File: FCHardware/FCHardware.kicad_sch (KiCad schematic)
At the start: 40 parts, among them J1 JST-8pin, J3 USB_C_Receptacle_USB2.0_16P, SW3 SW_Push, U2 MPU-6050, U4 TPSM63603, U5 ESC_Xrotor_65A_4in1, U8 ESP32-S3-MINI-1U, U9 USBLC6-2SC6

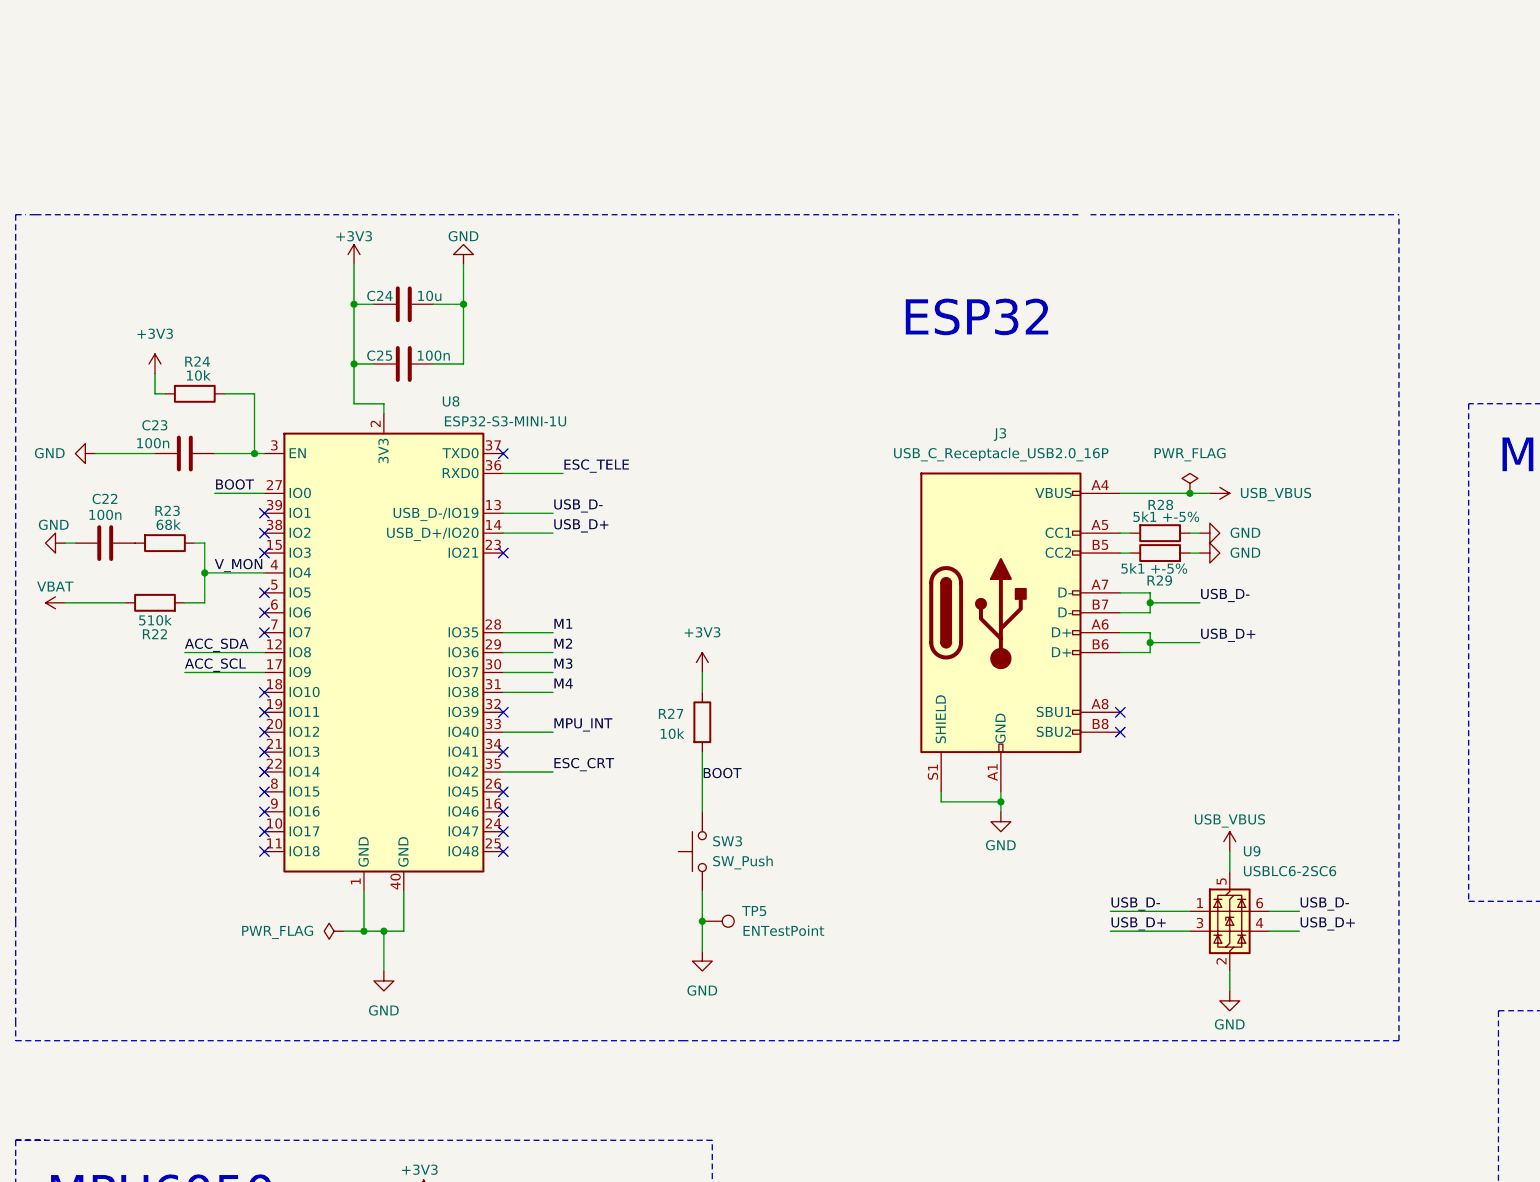
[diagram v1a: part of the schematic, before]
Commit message: Added actual references to capacitors and resistors
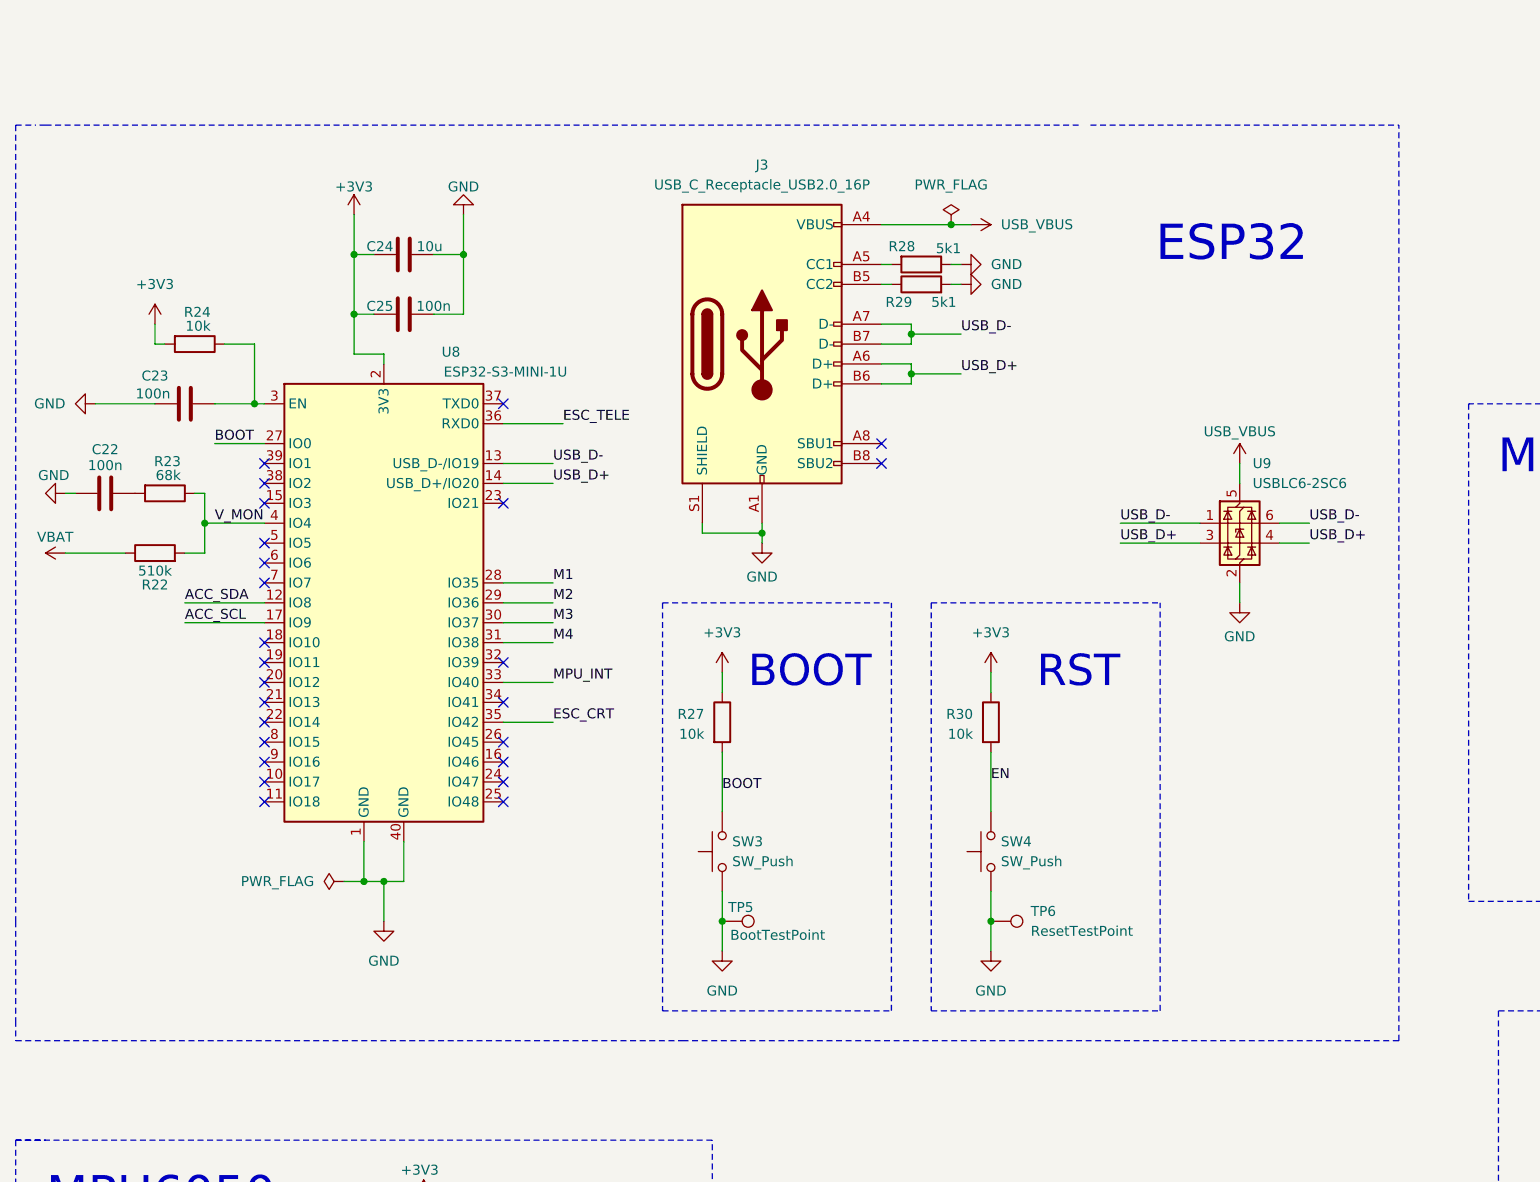
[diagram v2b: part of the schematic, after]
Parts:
- added R30: 10k, Resistor_SMD:R_0603_1608Metric_Pad0.98x0.95mm_HandSolder, symbol Device:R
- added SW4: SW_Push, Button_Switch_THT:SW_PUSH_6mm, symbol Switch:SW_Push
- added TP6: ResetTestPoint, TestPoint:TestPoint_Pad_D1.5mm, symbol Connector:TestPoint
- R28, R29: value 5k1 +-5% -> 5k1
- TP5: value ENTestPoint -> BootTestPoint
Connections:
- net +3V3: now also R30.1
- net GND: now also SW4.1, TP6.1
- new net EN: R30.2, SW4.2
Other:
- note added: "BOOT"
- note added: "RST"
- moved on the sheet: C22, C23, C24, C25, J3, R22, R23, R24, R27, R28, R29, SW3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

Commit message: Switched to STM mcu and ICM-42688 imu
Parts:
- removed C22, C23, C25, C8: 100n, Capacitor_SMD:C_0603_1608Metric_Pad1.08x0.95mm_HandSolder, symbol Device:C
- removed C24: 10u, Capacitor_SMD:C_0805_2012Metric_Pad1.18x1.45mm_HandSolder, symbol Device:C
- removed C7: 1u, Capacitor_SMD:C_0603_1608Metric_Pad1.08x0.95mm_HandSolder, symbol Device:C
- removed C9: 2n2, Capacitor_SMD:C_0603_1608Metric_Pad1.08x0.95mm_HandSolder, symbol Device:C
- removed R22: 510k, Resistor_SMD:R_0603_1608Metric_Pad0.98x0.95mm_HandSolder, symbol Device:R
- removed R23: 68k, Resistor_SMD:R_0603_1608Metric_Pad0.98x0.95mm_HandSolder, symbol Device:R
- removed R24: 10k, Resistor_SMD:R_0603_1608Metric_Pad0.98x0.95mm_HandSolder, symbol Device:R
- removed R7, R8: 2k2, Resistor_SMD:R_0603_1608Metric_Pad0.98x0.95mm_HandSolder, symbol Device:R
- removed U2: MPU-6050, Sensor_Motion:InvenSense_QFN-24_4x4mm_P0.5mm, symbol Sensor_Motion:MPU-6050
- removed U8: ESP32-S3-MINI-1U, RF_Module:ESP32-S3-WROOM-1U, symbol Custom_ESP32_Library:ESP32-S3-MINI-1U
- added C1, C3: 0u1, symbol Device:C
- added C2: 2u2, symbol Device:C
- added C26: 10u, Capacitor_SMD:C_0805_2012Metric_Pad1.18x1.45mm_HandSolder, symbol Device:C
- added C27, C28: 100n, Capacitor_SMD:C_0603_1608Metric_Pad1.08x0.95mm_HandSolder, symbol Device:C
- added R25: 510k, Resistor_SMD:R_0603_1608Metric_Pad0.98x0.95mm_HandSolder, symbol Device:R
- added R26: 68k, Resistor_SMD:R_0603_1608Metric_Pad0.98x0.95mm_HandSolder, symbol Device:R
- added U1: STM32F405RGTx, Package_QFP:LQFP-64_10x10mm_P0.5mm, symbol MCU_ST_STM32F4:STM32F405RGTx
- added U3: ICM-42688-P, ICM-42688-P:PQFN50P300X250X97-14N, symbol ICM-42688-P:ICM-42688-P
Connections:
- net +3V3: now also C1.2, C2.2, C26.2, C27.2, C3.1, U1.32 (VDD), U3.5 (VDDIO), U3.8 (VDD)
- net BOOT: now also U1.60 (BOOT0)
- net GND: now also C26.1, C27.1, C28.1
- net VBAT: now also R25.1
- net V_MON: now also R25.2, R26.1, U1.17 (PA3)
- new net: C28.2, R26.2
- new net ICU_INT: U3.4 (INT1/INT)
- new net ICU_SCL: U3.13 (AP_SCL/AP_SCLK)
- new net ICU_SDA: U3.14 (AP_SDA/AP_SDIO/AP_SDI)
- new net VSS: C1.1, C2.1, C3.2, U1.18 (VSS), U1.63 (VSS), U3.6 (GND), U3.7 (RESV_7)
- new net VSSA: U1.12 (VSSA)
- no-connect marks 42 -> 15
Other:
- note added: "IMU"
- note removed: "MPU6050"
- moved on the sheet: J3, R27, R28, R29, R30, SW3, SW4, TP5, TP6, U9

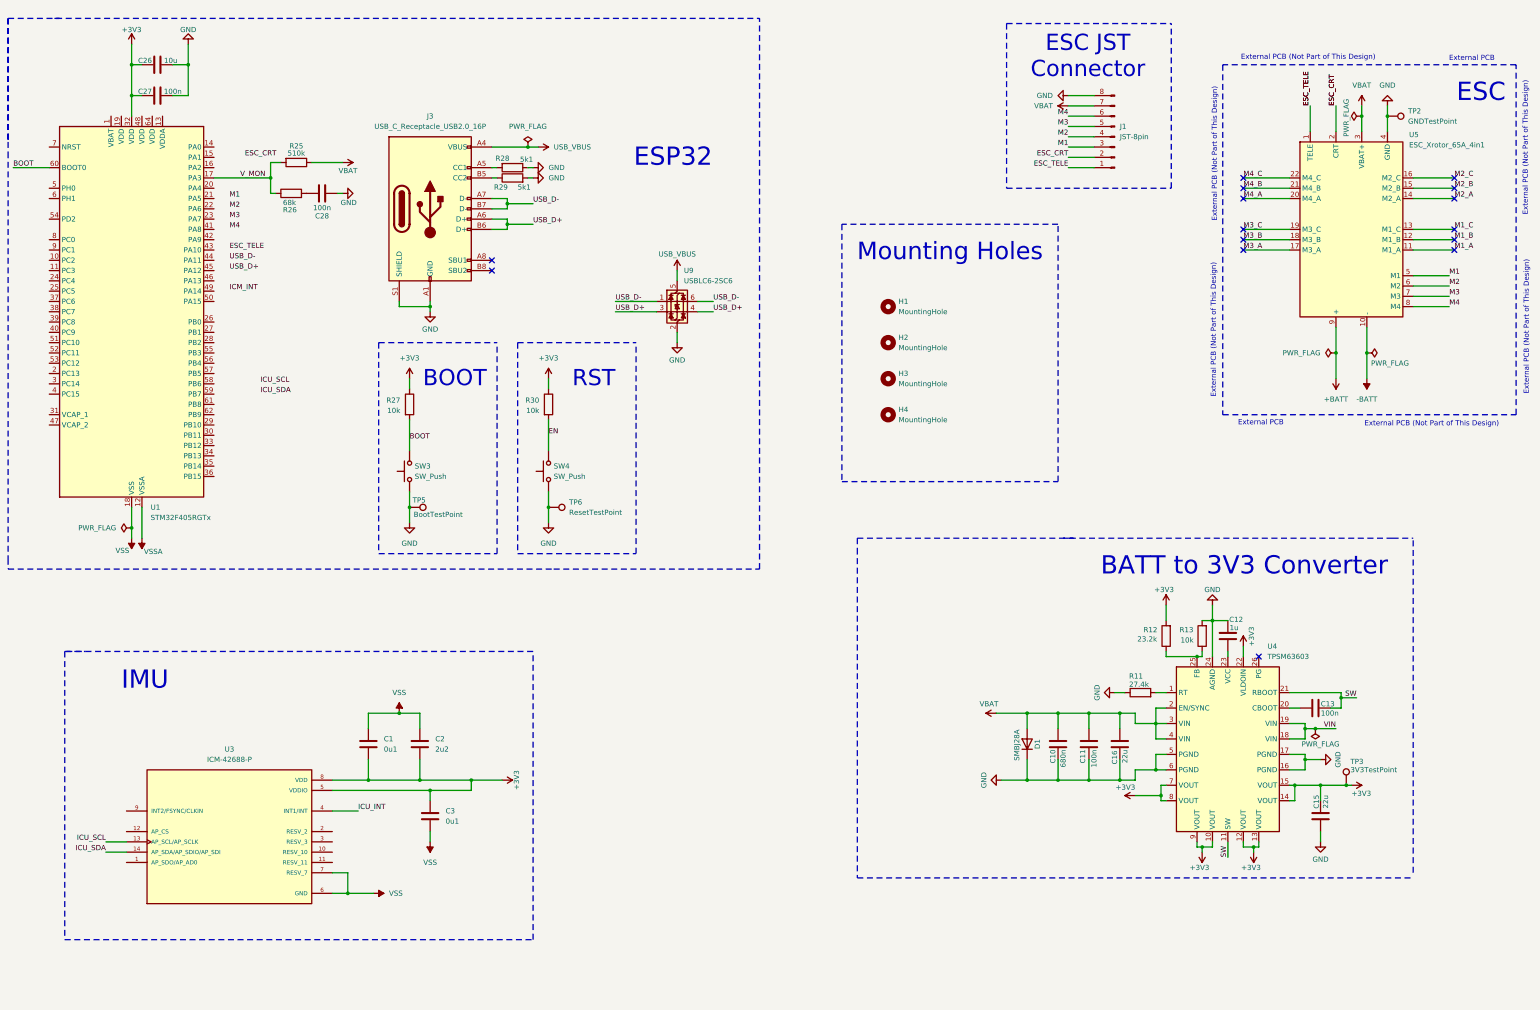
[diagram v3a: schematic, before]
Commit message: Added correct power management for STM32
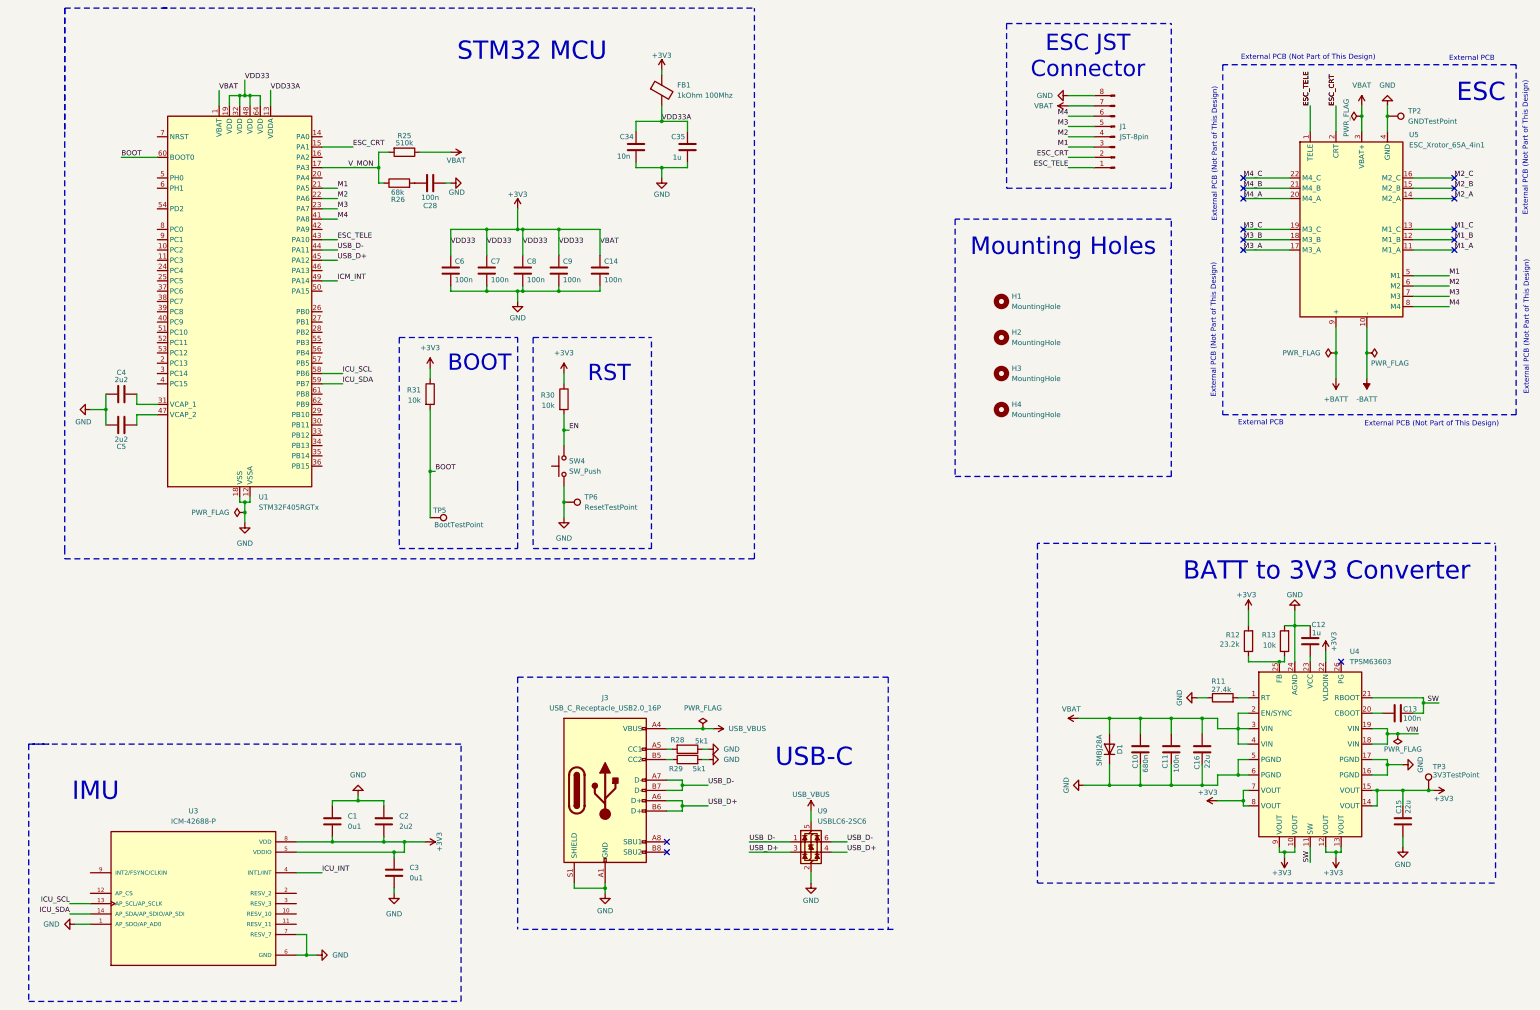
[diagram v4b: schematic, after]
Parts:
- removed C26: 10u, Capacitor_SMD:C_0805_2012Metric_Pad1.18x1.45mm_HandSolder, symbol Device:C
- removed C27: 100n, Capacitor_SMD:C_0603_1608Metric_Pad1.08x0.95mm_HandSolder, symbol Device:C
- removed R27: 10k, Resistor_SMD:R_0603_1608Metric_Pad0.98x0.95mm_HandSolder, symbol Device:R
- removed SW3: SW_Push, Button_Switch_THT:SW_PUSH_6mm, symbol Switch:SW_Push
- added C14, C6, C7, C8, C9: 100n, symbol Device:C
- added C34: 10n, Capacitor_SMD:C_0603_1608Metric_Pad1.08x0.95mm_HandSolder, symbol Device:C
- added C35: 1u, Capacitor_SMD:C_0603_1608Metric_Pad1.08x0.95mm_HandSolder, symbol Device:C
- added C4, C5: 2u2, symbol Device:C
- added FB1: 1kOhm 100Mhz, symbol Device:FerriteBead
- added R31: 10k, Resistor_SMD:R_0603_1608Metric_Pad0.98x0.95mm_HandSolder, symbol Device:R
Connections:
- net VBAT is gone; now on net +3V3: C10.2, C11.2, C16.2, D1.2 (A), J1.7 (Pin_7), R25.1, U4.2 (EN/SYNC), U4.3 (VIN), U4.4 (VIN), U5.3 (VBAT+)
- net VSS is gone; now on net GND: C1.1, C2.1, C3.2, U1.18 (VSS), U1.63 (VSS), U3.6 (GND), U3.7 (RESV_7)
- net VSSA is gone; now on net GND: U1.12 (VSSA)
- net +3V3: now also U1.1 (VBAT), U1.19 (VDD), U1.48 (VDD), U1.64 (VDD), C14.1, C6.1, C7.1, C8.1, C9.1, FB1.1, R31.1
- net BOOT: now also TP5.1, R31.2
- net ESC_CRT: now also U1.15 (PA1)
- net ESC_TELE: now also U1.43 (PA10)
- net GND: now also U3.1 (AP_SDO/AP_AD0), C14.2, C34.1, C35.1, C4.1, C5.2, C6.2, C7.2, C8.2, C9.2; no longer TP5.1
- net ICM_INT: now also U1.49 (PA14)
- net ICU_SCL: now also U1.58 (PB6)
- net ICU_SDA: now also U1.59 (PB7)
- net M1: now also U1.21 (PA5)
- net M2: now also U1.22 (PA6)
- net M3: now also U1.23 (PA7)
- net M4: now also U1.41 (PA8)
- net USB_D+: now also U1.45 (PA12)
- net USB_D-: now also U1.44 (PA11)
- net VDD33A: now reaches U1.13 (VDDA)
- net VDD33A: now also C34.2, C35.2, FB1.2
- net at U1.31 (VCAP_1): now also C4.2
- net at U1.47 (VCAP_2): now also C5.1
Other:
- note added: "STM32 MCU"
- note added: "USB-C"
- note removed: "ESP32"
- moved on the sheet: C1, C10, C11, C12, C13, C15, C16, C2, C28, C3, D1, H1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
